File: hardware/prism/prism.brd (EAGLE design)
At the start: 100 x 79 mm, 164 parts, among them IC1 MAX3232CSE, IC2 XMEGA128-A1, IC3 NCV78M05BDTRKG, IC4 LM25011MY, IC5 74LVC4245APW, IC6 74LVC4245APW, IC7 LM2731XMF, J3 794618-4, K1 LED_G, K2 LED_G, K3 LED_G, K4 LED_G, K5 LED_G, K6 LED_G, K7 LED_G, K8 LED_G, T1 NTGS4111PT1G, T2 MMBT2222LT1G, T3 MMBT2222LT1G, T4 NTGS4111PT1G, T5 MMBT2222LT1G, T6 MMBT2222LT1G, T8 MMBT2222LT1G, T9 NTGS4111PT1G

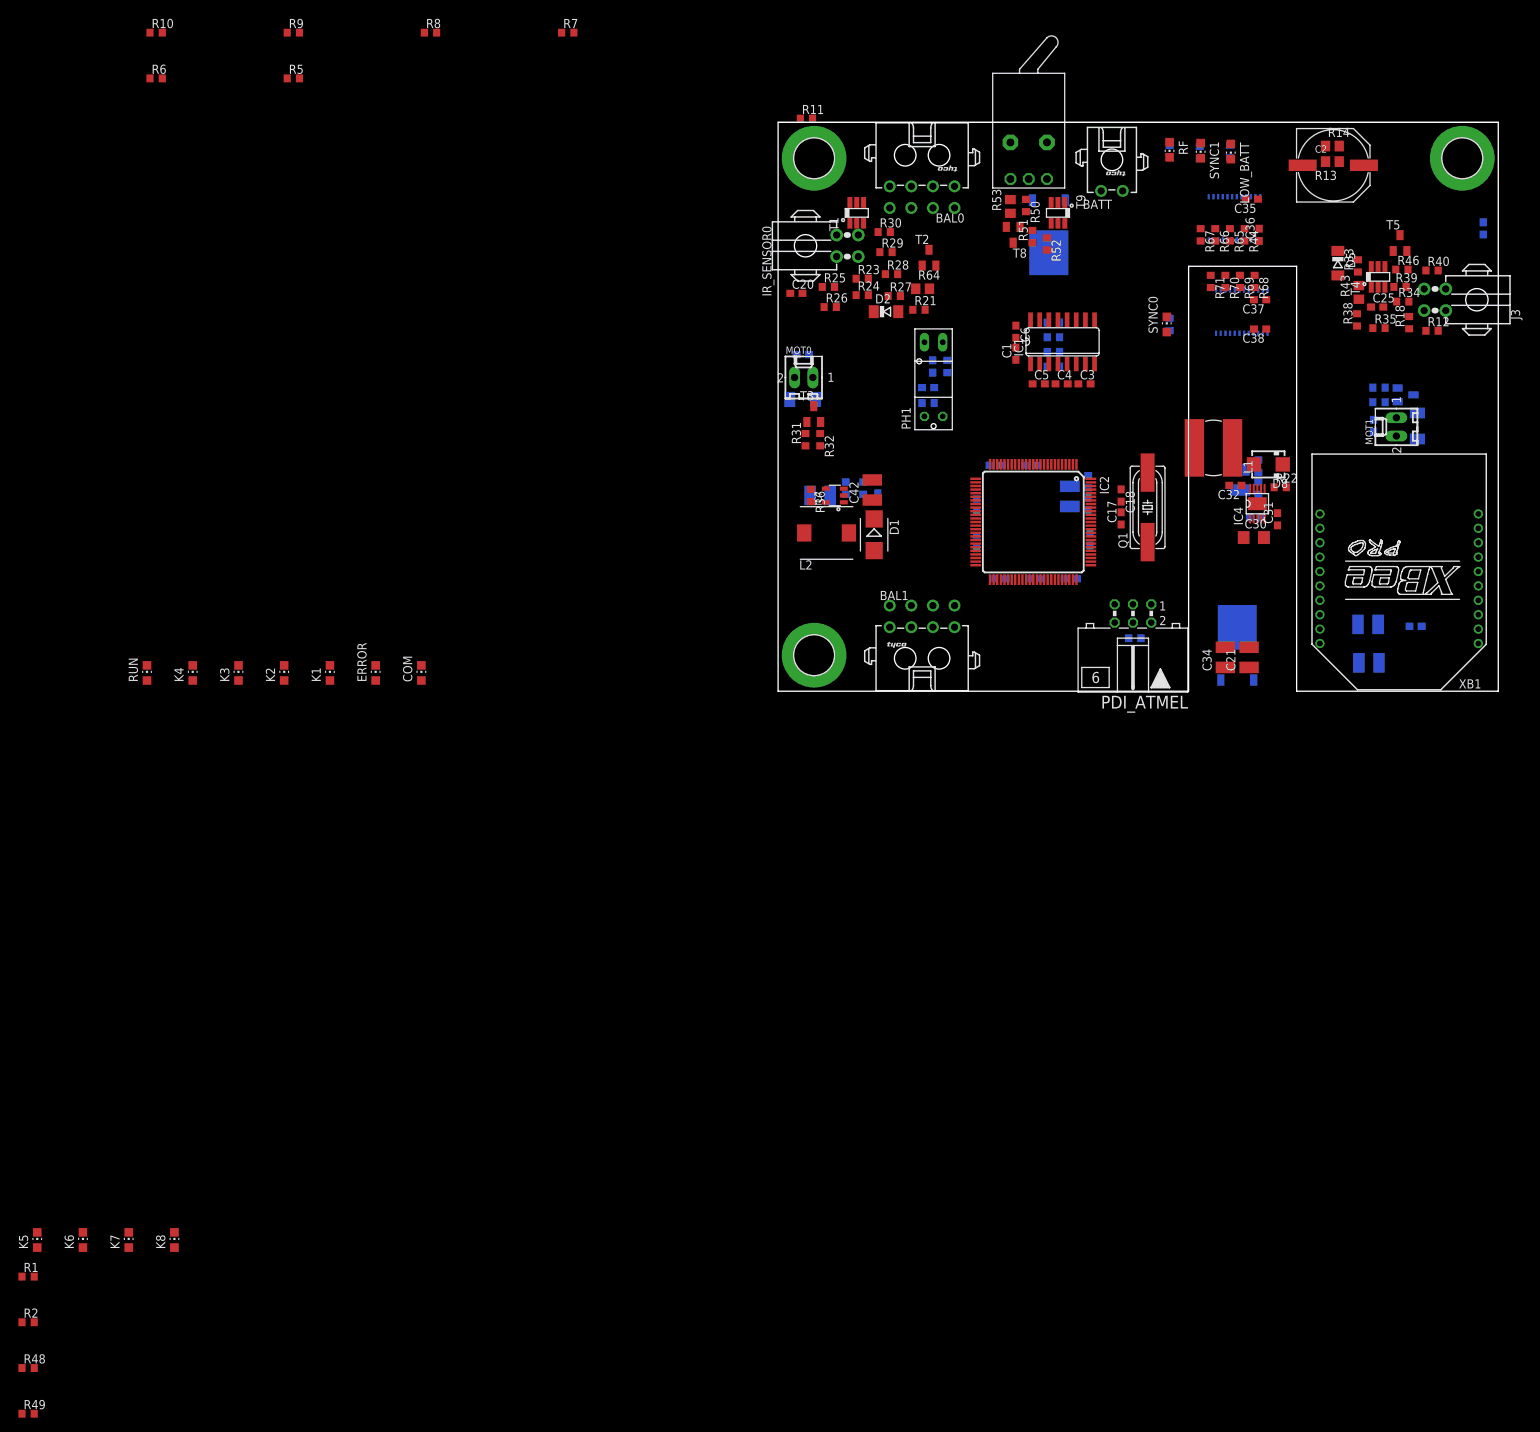
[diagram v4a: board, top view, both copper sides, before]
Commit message: added bluetooth board, begining of routing
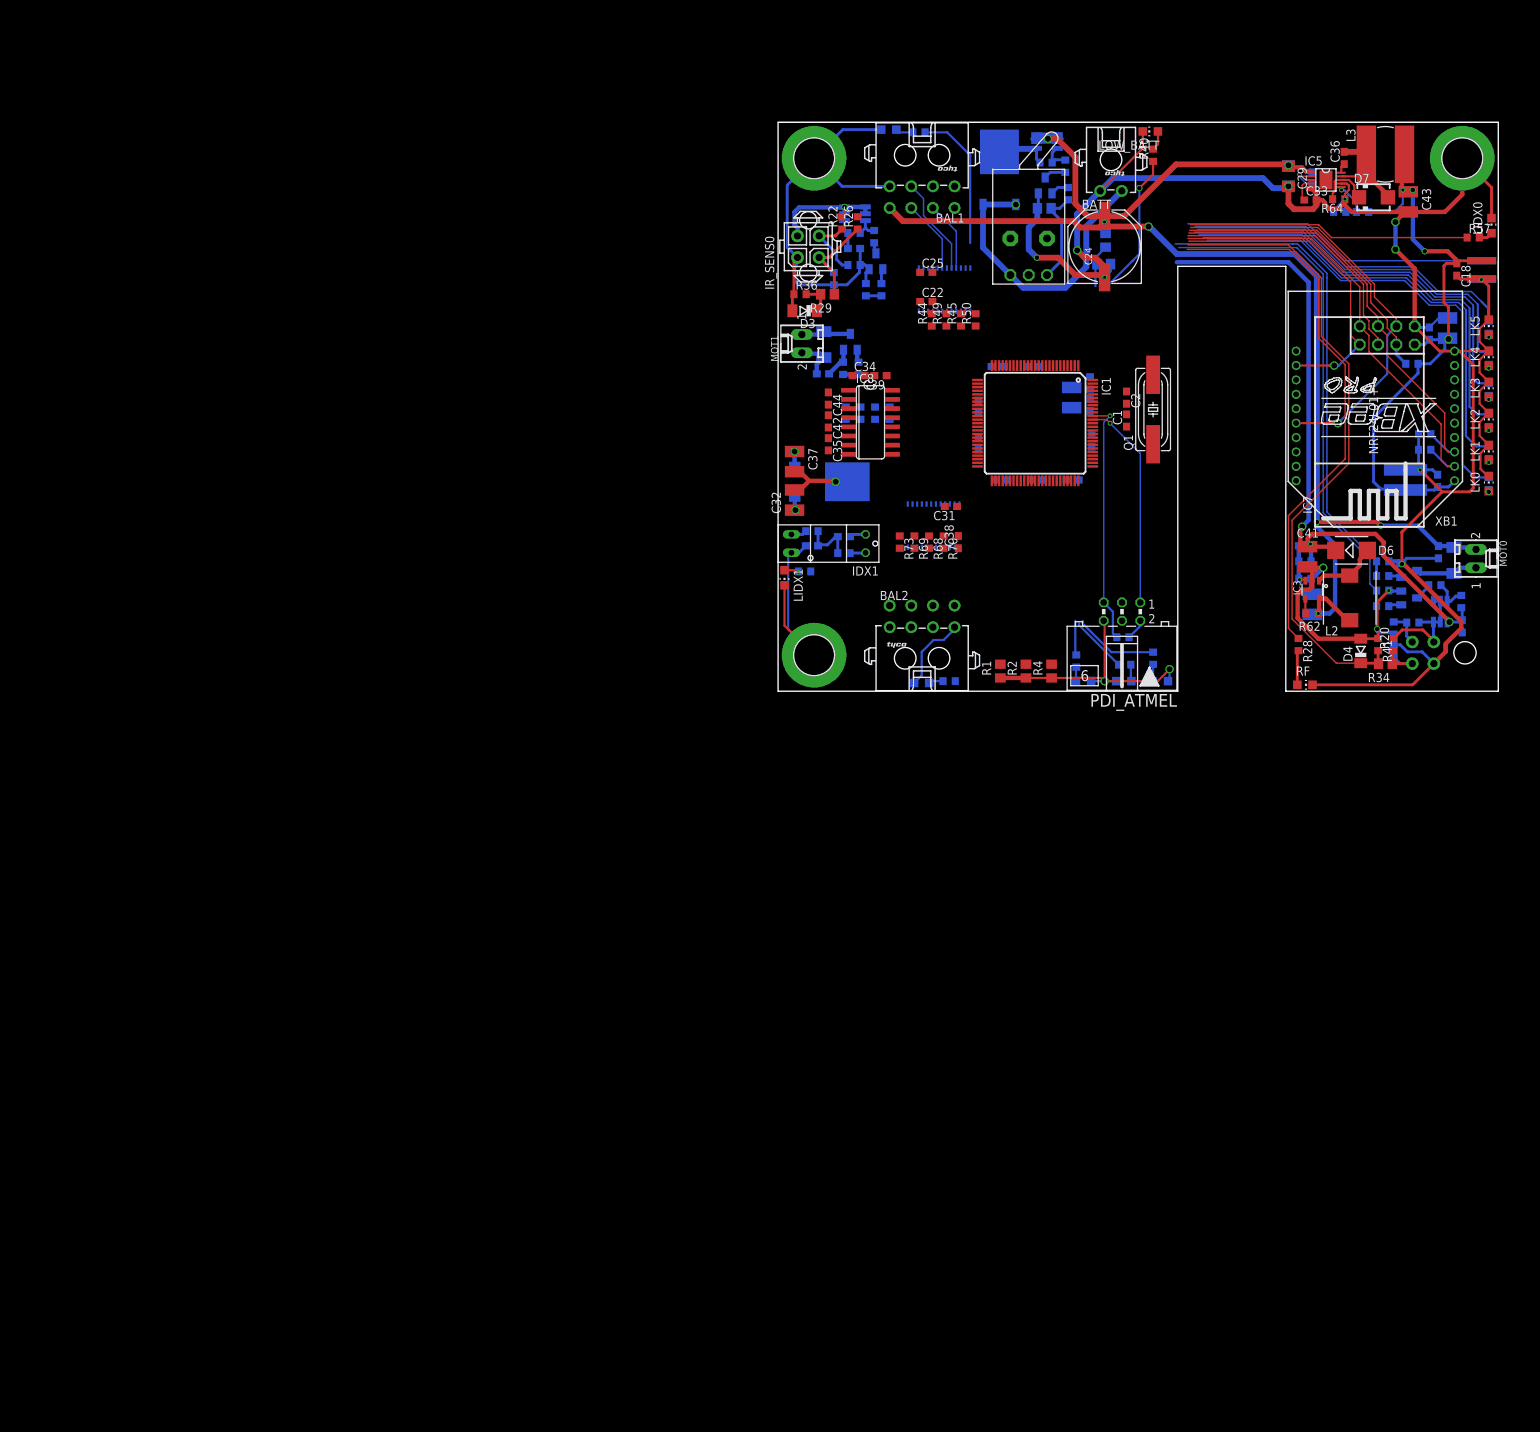
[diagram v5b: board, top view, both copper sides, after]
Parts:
- removed BAL0: 794618-8, robotter_connector:794618-8
- removed D8: B160-13F, robotter_diode:SMA
- removed IR_SENSOR0, J3: 794618-4, robotter_connector:794618-4
- removed K1, K2, K3, K4, K5, K6, K7, K8: LED_G, robotter_diode:CHIP-LED0805
- removed PH1: GP1S58VJ000F, robotter_ic:GP1S58VJ000F
- removed SYNC0: LED_B, robotter_diode:CHIP-LED0805
- removed T9: NTGS4111PT1G, robotter_ic:TSOP-6
- added BAL2: 794618-8, robotter_connector:794618-8
- added C26: 1µF 25V, robotter_capacitor:C1206
- added C44: 100nF 50V, robotter_capacitor:C0603
- added D4: bzv55-c3v3, robotter_diode:SOD80C
- added IC8: MAX3232CSE, robotter_ic:SO16
- added IDX0: PRISM_INDEX_EXTENSION_MALE, robotter_others:PRISM_INDEX_EXTENSION_MALE
- added IDX1: GP1S58VJ000F, robotter_ic:GP1S58VJ000F
- added IR_SENS0: 794681-4, robotter_connector:794681-4
- added IR_SENSOR1: 794618-4, robotter_connector:794618-4
- added LIDX0, LIDX1, LK0, LK1, LK2, LK3, LK4, LK5: LED_G, robotter_diode:CHIP-LED0805
- added R41: nc, rcl:R0603
- added R42, R72: 10K-F, robotter_resistor:R0603
- added R47, R59: 270-F, robotter_resistor:R0603
- added R73: 0-F, robotter_resistor:R0603
- added SYNC2: LED_B, robotter_diode:CHIP-LED0805
- added T7: MMBT2222LT1G, robotter_ic:SOT23-BEC
- C1: value 100nF 50V -> 15pF_0603_100V
- C15, C20, C32, C37: value 100nF 50V -> 10µF 25V; device robotter_capacitor:C0603 -> robotter_capacitor:C1210
- C17, C18: value 15pF_0603_100V -> 100nF 50V
- C2: value 330µF 35V -> 15pF_0603_100V; device robotter_capacitor:PANASONIC_G -> robotter_capacitor:C0603
- C22, C30: value 1µF 25V -> 100nF 50V; device robotter_capacitor:C1206 -> robotter_capacitor:C0603
- C24: value 100nF 50V -> 330µF 35V; device robotter_capacitor:C0603 -> robotter_capacitor:PANASONIC_G
- C29: value 100nF 50V -> 1µF 25V; device robotter_capacitor:C0603 -> robotter_capacitor:C1206
- C31: value 10nF 50V -> 100nF 50V
- C33: value 10µF 25V -> 10nF 50V; device robotter_capacitor:C1210 -> robotter_capacitor:C0603
- C34, C42, C8: value 10µF 25V -> 100nF 50V; device robotter_capacitor:C1210 -> robotter_capacitor:C0603
- C40: value 100nF 50V -> 180pF 50V
- C41: value 180pF 50V -> 10µF 25V; device robotter_capacitor:C0603 -> robotter_capacitor:C1210
- D1: value B120-13-F -> CGRM4004-G; device robotter_diode:SMB -> robotter_diode:SOD-123_MINI-SMA
- D2: value bzv55-c3v3 -> CGRM4004-G; device robotter_diode:SOD80C -> robotter_diode:SOD-123_MINI-SMA
- D3: value CGRM4004-G -> bzv55-c3v3; device robotter_diode:SOD-123_MINI-SMA -> robotter_diode:SOD80C
- D5: value bzv55-c3v3 -> (none); device robotter_diode:SOD80C -> robotter_diode:TO252
- D6: value CGRM4004-G -> B120-13-F; device robotter_diode:SOD-123_MINI-SMA -> robotter_diode:SMB
- D7: value (none) -> B160-13F; device robotter_diode:TO252 -> robotter_diode:SMA
- IC1: value MAX3232CSE -> XMEGA128-A1; device robotter_ic:SO16 -> avr-7:TQFP100
- IC2: value XMEGA128-A1 -> 74LVC4245APW; device avr-7:TQFP100 -> robotter_ic:TSSOP24
- IC3: value NCV78M05BDTRKG -> LM2731XMF; device linear:DPACK_3 -> robotter_ic:SOT23-5
- IC4: value LM25011MY -> 74LVC4245APW; device robotter_ic:MSOP10_THERMAL -> robotter_ic:TSSOP24
- IC5: value 74LVC4245APW -> LM25011MY; device robotter_ic:TSSOP24 -> robotter_ic:MSOP10_THERMAL
- IC6: value 74LVC4245APW -> NCV78M05BDTRKG; device robotter_ic:TSSOP24 -> linear:DPACK_3
- IC7: value LM2731XMF -> NRF24L01+; device robotter_ic:SOT23-5 -> robotter_ic:NRF24L01+
- L1: value SDR0805-270KL -> 220 ohms; device robotter_inductor:SDR0805 -> robotter_inductor:R0603
- L3: value 220 ohms -> SDR0805-270KL; device robotter_inductor:R0603 -> robotter_inductor:SDR0805
- R1, R2: value 270-F -> 0-E; device robotter_resistor:R0603 -> robotter_resistor:R0805
- R10, R11, R5, R54, R55, R7, R9: value 270-F -> 10K-F
- R12: value 0-F -> 1k
- R13: value 15k 1% -> 10K-F; device robotter_resistor:R0805 -> robotter_resistor:R0603
- R14: value 1k -> 10K-F; device robotter_resistor:R0805 -> robotter_resistor:R0603
- R16: value 4K7-F -> 1k
- R18: value 0-F -> 0; device robotter_resistor:R0603 -> rcl:R0603
- R19, R36: value 10K_1%-F -> nc; device robotter_resistor:R0603 -> rcl:R0603
- R20: value 113K-F -> 10K-F
- R22: value 0.27-F -> 0-F
- R23: value 10K-F -> 0-F
- R24: value 10K-F -> 4K7-F
- R25: value 0 -> 270-F; device rcl:R0603 -> robotter_resistor:R0603
- R27: value 1k -> nc; device robotter_resistor:R0603 -> rcl:R0603
- R28: value nc -> 270-F; device rcl:R0603 -> robotter_resistor:R0603
- R29, R34: value nc -> 4K7-E; device rcl:R0603 -> robotter_resistor:R0805
- R31, R38: value 1k -> 270-F
- R32, R35, R40, R52: value 10K-F -> 270-F
- R33: value nc -> 10K-F; device rcl:R0603 -> robotter_resistor:R0603
- R4: value 10K-F -> 0-E; device robotter_resistor:R0603 -> robotter_resistor:R0805
- R43: value 4K7-E -> 10K-F; device robotter_resistor:R0805 -> robotter_resistor:R0603
- R45: value 1k -> 0-F
- R46: value 10K-F -> 10K-E; device robotter_resistor:R0603 -> robotter_resistor:R0805
- R49: value 270-F -> 0-F
- R50: value 1K-F -> 0-F
- R51: value 10K-F -> 1K-F
- R53: value 10K-E -> 270-F; device robotter_resistor:R0805 -> robotter_resistor:R0603
- R58: value 75K-F -> 270-F
- R6, R8: value 270-F -> 1k
- R60: value 10K-F -> 15k 1%; device robotter_resistor:R0603 -> robotter_resistor:R0805
- R61: value 3K09-F -> 1k; device robotter_resistor:R0603 -> robotter_resistor:R0805
- R62: value 10K-F -> 10K_1%-F
- R63: value 10K-F -> 75K-F
- R64: value 4K7-E -> 0.27-F; device robotter_resistor:R0805 -> robotter_resistor:R0603
- R65: value 0-F -> 113K-F
- R66: value 0-F -> 10K_1%-F
- R67: value 0-F -> 10K-F
- R71: value 0-F -> 3K09-F
- T1, T4: value NTGS4111PT1G -> MMBT2222LT1G; device robotter_ic:TSOP-6 -> robotter_ic:SOT23-BEC
- T2, T5, T8: value MMBT2222LT1G -> NTGS4111PT1G; device robotter_ic:SOT23-BEC -> robotter_ic:TSOP-6
- moved R48 246.6 mm to (98.7, 46.2), flipped to the bottom, turned to 270 degrees
- moved R49 198.3 mm to (23.4, 51.6), turned to 90 degrees
- moved R10 193.4 mm to (91.2, 14.7), flipped to the bottom, turned to 180 degrees
- moved R6 185.4 mm to (83.9, 11.8), flipped to the bottom, turned to 180 degrees
- moved R9 180.4 mm to (94.9, 12.4), flipped to the bottom, turned to 270 degrees
- moved R5 167.1 mm to (83.9, 14.0), flipped to the bottom
- moved R2 165.5 mm to (34.4, 2.79), turned to 90 degrees
- moved R1 159.0 mm to (30.9, 2.79), turned to 90 degrees
- moved RUN 135.6 mm to (48.0, 1.40), flipped to the bottom, turned to 270 degrees
- moved COM 102.6 mm to (53.1, 1.40), flipped to the bottom, turned to 90 degrees
- moved ERROR 98.3 mm to (42.4, 1.40), flipped to the bottom, turned to 90 degrees
- moved MOT0 96.7 mm to (96.9, 18.4), turned to 270 degrees
- moved T1 93.5 mm to (87.6, 13.0), flipped to the bottom, turned to 90 degrees
- moved C43 91.3 mm to (87.5, 67.9), flipped to the top, turned to 270 degrees
- moved C23 89.9 mm to (91.6, 29.2), turned to 90 degrees
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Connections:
- removed net LED_SOUTH: IC2.68, R49.1, R8.1
- removed net N$21: K7.A, R48.2
- removed net N$93: K3.A, R7.2
- removed net XBEE_CTS_3V3: IC2.57, XB1.12
- removed net XBEE_RTS_3V3: IC2.58, XB1.16
- removed net XBEE_RX_3V3: IC2.31, XB1.2
- removed net XBEE_TX_3V3: IC2.32, XB1.3
- new net BEACON_ID_0_3V3: IC1.5, R1.2
- new net BEACON_ID_1_3V3: IC1.6, R2.2
- new net BEACON_ID_2_3V3: IC1.7, R4.2
- new net LED_INDEX_0_3V3: IC1.81, R57.1
- new net LED_INDEX_1_3V3: IC1.82, R59.1
- new net LK0_3V3: IC1.75, R47.1
- new net LK1: LK2.A, R56.2
- new net LK1_3V3: IC1.76, R52.1
- new net LK2_3V3: IC1.77, R56.1
- new net LK3_3V3: IC1.78, R58.1
- new net LK4_3V3: IC1.79, R48.1
- new net LK5: LIDX0.A, R57.2
- new net LK5_3V3: IC1.80, R53.1
- new net NRF_CSN_3V3: IC1.35, IC7.4, R67.1
- new net NRF_MOSI_3V3: IC1.30, IC7.6
- new net XBEE_CTS_3V3/NRF_IRQ_3V3: IC1.57, IC7.8, XB1.12
- new net XBEE_RTS_3V3/NRF_CE_3V3: IC1.58, IC7.3, XB1.16
- new net XBEE_RX_3V3/NRF_MISO_3V3: IC1.31, IC7.7, R43.2, XB1.2
- new net XBEE_TX_3V3/NRF_SCK_3V3: IC1.32, IC7.5, R42.2, XB1.3
- net +15V: now also C3.1, C4.1, C40.1, D6.C, R14.2, R65.1, R9.2, T2.4, T5.4; no longer C20.1, C25.1, C42.1, D1.C, R20.1, R24.2, R46.2, T1.4, T4.4
- net +3V3: now also C17.1, C18.1, C20.1, C21.1, C22.1, C23.1, C30.1, C31.1, C43.1, C5.1, C8.1, IC1.14, IC1.24, IC1.34, IC1.44, IC1.54, IC1.64, IC1.74, IC1.83, IC2.2, IC2.23, IC4.23, IC4.24, IC7.2, IC8.16, IDX0.2, R24.2, R3.1, R30.1, R33.1, R37.2, R39.2, R67.2, R71.1; no longer C10.1, C15.1, C28.1, C29.1, C33.1, C35.1, C37.1, C40.1, C6.1, IC1.16, IC2.14, IC2.34, IC2.44, IC2.54, IC2.64, IC2.74, IC2.83, IC5.2, IC5.23, IC5.24, IC6.23, IC6.24, R15.1, R16.2, R3.2, R4.2, R61.1, R62.1, R63.1
- net +5V: now also C25.1, C37.1, IC2.1, IC4.1, IC6.3; no longer C34.1, C36.1, IC3.3, IC5.1, IC6.1
- net /RESET_3V3: now also IC1.90, R3.2; no longer IC2.90, R15.2
- net BATTERY_MONITOR_0-1V: now also IC1.97, R60.1, R61.2; no longer IC2.97, R13.1, R14.2
- net GND: now also BAL2.1, C2.2, C24.-, C26.2, C32.2, C4.2, C41.2, C5.2, D3.A, D4.A, IC1.13, IC1.23, IC1.3, IC1.33, IC1.43, IC1.53, IC1.63, IC1.73, IC1.84, IC1.93, IC2.11, IC2.12, IC2.22, IC3.2, IC4.11, IC4.12, IC4.13, IC4.2, IC4.22, IC5.5, IC5.7, IC6.4, IC7.1, IC8.15, IDX0.1, IDX0.3, IDX1.LED_C, IDX1.TRANSISTOR_E, IR_SENS0.1, IR_SENSOR1.1, LIDX0.C, LIDX1.C, LK0.C, LK1.C, LK2.C, LK3.C, LK4.C, LK5.C, R1.1, R11.1, R13.1, R2.1, R23.1, R27.1, R36.1, R4.1, R41.1, R42.1, R43.1, R46.1, R5.1, R61.1, R64.1, R66.1, R7.1, R72.2, SYNC2.C, T1.E, T4.E, T7.E; no longer BAL0.1, C2.-, C24.2, C36.2, C40.2, C42.2, D2.A, D5.A, IC1.15, IC2.23, IC2.3, IC2.33, IC2.43, IC2.53, IC2.63, IC2.73, IC2.84, IC2.93, IC3.4, IC4.5, IC4.7, IC5.11, IC5.12, IC5.13, IC5.22, IC6.11, IC6.12, IC6.13, IC6.2, IC6.22, IC7.2, IR_SENSOR0.1, J3.1, K1.C, K2.C, K3.C, K4.C, K5.C, K6.C, K7.C, K8.C, PH1.LED_C, PH1.TRANSISTOR_E, R14.1, R18.1, R22.1, R28.1, R29.1, R30.1, R32.1, R33.1, R34.1, R35.1, R37.1, R53.1, R60.2, SYNC0.C, T2.E, T5.E, T8.E
- net INT0_0_3V3: now also IC4.16, R50.1; no longer IC6.16, R71.1
- net INT0_0_5V: now also BAL1.2, IC2.8, R73.2; no longer BAL0.2, IC5.8, R67.2
- net INT0_1_3V3: now also IC4.17, R45.1; no longer IC6.17, R70.1
- net INT0_1_5V: now also BAL2.2, IC2.7, R69.2; no longer BAL1.2, IC5.7, R66.2
- net INT1_0_3V3: now also IC4.18, R49.1; no longer IC6.18, R69.1
- net INT1_0_5V: now also BAL1.6, IC2.6, R68.2; no longer BAL0.6, IC5.6, R65.2
- net INT1_1_3V3: now also IC4.19, R44.1; no longer IC6.19, R68.1
- net INT1_1_5V: now also BAL2.6, IC2.5, R70.2; no longer BAL1.6, IC5.5, R44.2
- net IR_SENSOR_0_OUTPUT_24V: now also IR_SENSOR1.2, R20.1, R21.2, R34.1; no longer IR_SENSOR0.2, R23.1, R28.2, R64.1
- net IR_SENSOR_0_OUTPUT_3V3: now also D3.C, IC1.17, R29.2, R36.2; no longer D2.C, IC2.17, R21.2, R64.2
- net IR_SENSOR_1_OUTPUT_24V: now also IR_SENS0.2, R26.1, R27.2, R29.1; no longer J3.2, R34.2, R39.1, R43.1
- net IR_SENSOR_1_OUTPUT_3V3: now also D4.C, IC1.37, R34.2, R41.2; no longer D5.C, IC2.37, R33.2, R43.2
- net LED_EAST: now also IC1.56; no longer IC2.56, R2.1, R6.1
- net LED_NORTH: now also IC1.62; no longer IC2.62, R1.1, R5.1
- net LED_WEST: now also IC1.95; no longer IC2.95, R48.1, R7.1
- net MIRROR_INDEX_0_3V3: now also IC1.18, IDX0.4; no longer IC2.18, PH1.TRANSISTOR_C, R16.1
- net MIRROR_INDEX_1_3V3: now also IC1.38, IDX1.TRANSISTOR_C, R24.1; no longer IC2.38
- net MOTOR_M_0: now also D2.A, T6.C; no longer D3.A, T3.C
- net MOTOR_M_1: now also D1.A, T4.C; no longer D6.A, T6.C
- net MOTOR_PWM_0_3V3: now also IC1.25, R13.2, R16.1; no longer IC2.25, R31.1, R32.2
- net MOTOR_PWM_1_3V3: now also IC1.26, R11.2, R12.1; no longer IC2.26, R37.2, R45.1
- net N$1: now also C44.1, IC8.1; no longer C5.1, IC1.1
- net N$10: now also IC1.71, R31.1; no longer IC2.76, R10.1
- net N$11: now also C34.1, IC8.2; no longer C1.1, IC1.2
- net N$12: now also IC1.72, R35.1; no longer IC2.77, R11.1
- net N$128: now also R10.2, R9.1, T2.3; no longer R24.1, R26.2, T1.3
- net N$129: now also IR_SENSOR1.4, R18.1, R19.2; no longer IR_SENSOR0.4, R25.1, R29.2
- net N$13: now also C35.1, IC8.6; no longer C3.1, IC1.6
- net N$14: now also R14.1, R15.2, T5.3; no longer R40.2, R46.1, T4.3
- net N$16: now also R8.2, T3.B; no longer R38.2, T5.B
- net N$17: now also R15.1, T3.C; no longer R40.1, T5.C
- net N$18: now also R16.2; no longer R45.2
- net N$19: now also LK0.A, R47.2; no longer K5.A, R1.2
- net N$2: now also R25.2; no longer R9.2
- net N$20: now also LK1.A, R52.2; no longer K6.A, R2.2
- net N$22: now also LK3.A, R58.2; no longer K8.A, R49.2
- net N$23: now also D5.1, D5.3, SW_BATT.1; no longer D7.1, D7.3, SW_BATT.2
- net N$24: now also C42.2, IC8.5; no longer C4.2, IC1.5
- net N$25: now also R51.2, T7.B; no longer R50.2, T8.B
- net N$26: now also R54.1, R55.2, T8.3; no longer R51.2, R52.1, T9.3
- net N$27: now also R28.2; no longer R54.2
- net N$28: now also IC1.65, R28.1; no longer IC2.69, R54.1
- net N$29: now also R55.1, T7.C; no longer R51.1, T8.C
- net N$3: now also R12.2, T4.B; no longer R31.2, T3.B
- net N$30: now also D5.4, R54.2, T8.4; no longer D7.4, R52.2, T9.4
- net N$31: now also IC1.67, R38.2; no longer IC2.71, R55.2
- net N$32: now also IC1.68, R40.1; no longer IC2.72, R56.1
- net N$33: now also R38.1, SYNC2.A; no longer R55.1, SYNC1.A
- net N$34: now also R40.2; no longer R56.2
- net N$35: now also R32.1, SYNC1.A; no longer R57.1, SYNC0.A
- net N$36: now also IC1.66, R32.2; no longer IC2.70, R57.2
- net N$37: now also R6.2, T1.B; no longer R27.2, T2.B
- net N$38: now also C36.2, D7.A, IC5.9, L3.1; no longer C32.2, D8.A, IC4.9, L1.1
- net N$39: now also D7.C, IC5.8, R64.2; no longer D8.C, IC4.8, R22.2
- net N$4: now also R31.2; no longer R10.2
- net N$40: now also IC5.2, R63.1; no longer IC4.2, R58.1
- net N$41: now also IR_SENS0.4, R22.1, R23.2; no longer J3.4, R12.1, R18.2
- net N$42: now also R10.1, T1.C; no longer R26.1, T2.C
- net N$43: now also C33.1, IC5.4; no longer C31.1, IC4.4
- net N$44: now also IC5.6, R71.2, R72.1; no longer IC4.6, R60.1, R61.2
- net N$45: now also C1.1, IC1.91; no longer C17.1, IC2.91
- net N$46: now also C2.1, IC1.92; no longer C18.1, IC2.92
- net N$47: now also IC4.5, R70.1; no longer IC6.5, R44.1
- net N$48: now also C36.1, IC5.10; no longer C32.1, IC4.10
- net N$49: now also IC2.19, R44.2; no longer IC5.19, R68.2
- net N$5: now also C44.2, IC8.3; no longer C5.2, IC1.3
- net N$50: now also IC2.17, R45.2; no longer IC5.17, R70.2
- net N$51: now also IC2.18, R49.2; no longer IC5.18, R69.2
- net N$52: now also IC2.16, R50.2; no longer IC5.16, R71.2
- net N$53: now also IC4.6, R68.1; no longer IC6.6, R65.1
- net N$54: now also IC4.8, R73.1; no longer IC6.8, R67.1
- net N$55: now also IC4.7, R69.1; no longer IC6.7, R66.1
- net N$56: now also IR_SENSOR1.3, R18.2, R20.2, T2.1, T2.2, T2.5, T2.6; no longer IR_SENSOR0.3, R23.2, R25.2, T1.1, T1.2, T1.5, T1.6
- net N$57: now also IDX1.LED_A; no longer PH1.LED_A
- net N$58: now also IR_SENS0.3, R22.2, R26.2, T5.1, T5.2, T5.5, T5.6; no longer J3.3, R12.2, R39.2, T4.1, T4.2, T4.5, T4.6
- net N$59: now also D6.A, IC3.1; no longer D1.A, IC7.1
- net N$6: now also C42.1, IC8.4; no longer C4.1, IC1.4
- net N$60: now also C40.2, IC3.3, R65.2, R66.2; no longer C41.2, IC7.3, R19.2, R20.2
- net N$63: now also IC3.4, R62.1; no longer IC7.4, R36.1
- net N$7: now also R35.2; no longer R11.2
- net N$8: now also C10.1, C15.1, IC1.4, IC1.94, L1.1; no longer C7.1, C8.1, IC2.4, IC2.94, L3.1
- net N$9: now also IC1.70, R25.1; no longer IC2.75, R9.1
- net N$91: now also LK4.A, R48.2; no longer K1.A, R5.2
- net N$92: now also LK5.A, R53.2; no longer K2.A, R6.2
- net N$94: now also LIDX1.A, R59.2; no longer K4.A, R8.2
- net ON/OFF_SENSOR_0_3V3: now also IC1.27, R7.2, R8.1; no longer IC2.28, R27.1, R30.2
- net ON/OFF_SENSOR_1_3V1: now also R46.2, R51.1, SW_BATT.3; no longer R50.1, R53.2, SW_BATT.1
- net ON/OFF_SENSOR_1_3V3: now also IC1.28, R5.2, R6.1; no longer IC2.29, R35.2, R38.1
- net PDI_DATA_3V3: now also IC1.89; no longer IC2.89
- net RX_0_3V3: now also IC1.51, IC8.12, R37.1; no longer IC1.12, IC2.51, R3.1
- net RX_0_RS232: now also BAL1.8, IC8.13; no longer BAL0.8, IC1.13
- net RX_1_3V3: now also IC1.47, IC8.9, R30.2; no longer IC1.9, IC2.47, R62.2
- net RX_1_RS232: now also BAL2.8, IC8.8; no longer BAL1.8, IC1.8
- net SYNC_IN_0_3V3: now also IC1.19, IC2.15; no longer IC2.19, IC5.15
- net SYNC_IN_0_5V: now also BAL1.7, IC2.9; no longer BAL0.7, IC5.9
- net SYNC_IN_1_3V3: now also IC1.20, IC2.14; no longer IC2.20, IC5.14
- net SYNC_IN_1_5V: now also BAL2.7, IC2.10; no longer BAL1.7, IC5.10
- net SYNC_OUT_0_3V3: now also IC1.21, IC4.15; no longer IC2.21, IC6.15
- net SYNC_OUT_0_5V: now also BAL1.3, IC4.9; no longer BAL0.3, IC6.9
- net SYNC_OUT_1_3V3: now also IC1.22, IC4.14; no longer IC2.22, IC6.14
- net SYNC_OUT_1_5V: now also BAL2.3, IC4.10; no longer BAL1.3, IC6.10
- net TX_0_3V3: now also IC1.52, IC8.11, R39.1; no longer IC1.11, IC2.52, R4.1
- net TX_0_RS232: now also BAL1.4, IC8.14; no longer BAL0.4, IC1.14
- net TX_1_3V3: now also IC1.48, IC8.10, R33.2; no longer IC1.10, IC2.48, R63.2
- net TX_1_RS232: now also BAL2.4, IC8.7; no longer BAL1.4, IC1.7
- net VBAT: now also BAL2.5, C24.+, C26.1, C28.1, C29.1, C32.1, C6.1, C7.1, D1.C, D2.C, IC3.5, IC5.1, IC6.1, R60.2, R62.2, R63.2, T8.1, T8.2, T8.5, T8.6; no longer BAL0.5, C2.+, C21.1, C22.1, C23.1, C24.1, C30.1, C43.1, D3.C, D6.C, IC3.1, IC4.1, IC7.5, R13.2, R36.2, R58.2, T9.1, T9.2, T9.5, T9.6
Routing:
- net GND: track 0.00 -> 520.7 mm, vias 0 -> 16
- net VBAT: track 0.00 -> 223.9 mm, vias 0 -> 8
- net +15V: track 0.00 -> 99.9 mm, vias 0 -> 3
- net +3V3: track 0.00 -> 94.9 mm, vias 0 -> 4
- net IR_SENSOR_1_OUTPUT_3V3: track 0.00 -> 89.0 mm
- net N$28: track 0.00 -> 75.3 mm
- net ON/OFF_SENSOR_1_3V3: track 0.00 -> 70.8 mm
- net MOTOR_PWM_0_3V3: track 0.00 -> 67.7 mm
- net LK0_3V3: track 0.00 -> 65.2 mm
- net LK1_3V3: track 0.00 -> 61.9 mm
- net XBEE_RX_3V3/NRF_MISO_3V3: track 0.00 -> 61.8 mm
- net XBEE_TX_3V3/NRF_SCK_3V3: track 0.00 -> 60.8 mm
- net LK2_3V3: track 0.00 -> 58.6 mm
- net XBEE_RTS_3V3/NRF_CE_3V3: track 0.00 -> 58.5 mm, vias 0 -> 1
- net LK3_3V3: track 0.00 -> 55.5 mm
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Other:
- outline, holes or cut-outs redrawn

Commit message: bord routed, ready to review
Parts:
- moved R70 13.5 mm to (14.0, 30.7), flipped to the bottom, turned to 90 degrees
- moved R68 11.2 mm to (16.0, 30.7), flipped to the bottom, turned to 90 degrees
- moved R73 10.5 mm to (20.1, 30.7), flipped to the bottom, turned to 90 degrees
- moved R69 10.1 mm to (18.0, 30.7), flipped to the bottom, turned to 90 degrees
- moved R37 6.48 mm to (9.02, 38.5)
- moved R30 3.69 mm to (15.1, 38.5)
- moved R33 3.69 mm to (13.1, 38.5)
- moved R20 3.58 mm to (85.1, 2.92), turned to 0 degrees
- moved R34 2.95 mm to (85.6, 6.48), turned to 90 degrees
- moved R22 2.90 mm to (7.11, 67.3), turned to 0 degrees
- moved R44 2.73 mm to (20.1, 49.1), flipped to the bottom
- moved R45 2.73 mm to (24.1, 49.1), flipped to the bottom
- moved R49 2.73 mm to (22.1, 49.1), flipped to the bottom
- moved R50 2.73 mm to (26.2, 49.1), flipped to the bottom
- moved R39 2.42 mm to (11.0, 38.5)
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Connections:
- removed net LED_EAST: IC1.56
- removed net LED_NORTH: IC1.62
- removed net LED_WEST: IC1.95
- removed net N$32: IC1.68, R40.1
- removed net N$36: IC1.66, R32.2
- new net LOW_BAT_LED_3V3: IC1.36, R40.1
- new net SYNC1_LED_3V3: IC1.35, R32.2
- net BEACON_ID_0_3V3: now also IC1.57; no longer IC1.5
- net BEACON_ID_1_3V3: now also IC1.58; no longer IC1.6
- net BEACON_ID_2_3V3: now also IC1.59; no longer IC1.7
- net INT0_0_3V3: now also IC1.39, IC4.17; no longer IC4.16
- net INT0_1_3V3: now also IC1.40, IC4.16; no longer IC4.17
- net INT1_0_3V3: now also IC1.41, IC4.15; no longer IC4.18
- net INT1_1_3V3: now also IC1.42, IC4.14; no longer IC4.19
- net IR_SENSOR_0_OUTPUT_3V3: now also IC1.30; no longer IC1.17
- net IR_SENSOR_1_OUTPUT_3V3: now also IC1.15; no longer IC1.37
- net LED_INDEX_0_3V3: now also IC1.6; no longer IC1.81
- net LED_INDEX_1_3V3: now also IC1.55; no longer IC1.82
- net LK0_3V3: now also IC1.7; no longer IC1.75
- net LK1_3V3: now also IC1.8; no longer IC1.76
- net LK2_3V3: now also IC1.9; no longer IC1.77
- net LK3_3V3: now also IC1.10; no longer IC1.78
- net LK4_3V3: now also IC1.11; no longer IC1.79
- net LK5_3V3: now also IC1.12; no longer IC1.80
- net MIRROR_INDEX_0_3V3: now also IC1.29; no longer IC1.18
- net MIRROR_INDEX_1_3V3: now also IC1.18, IC1.19; no longer IC1.38
- net N$10: now also IC1.60; no longer IC1.71
- net N$12: now also IC1.62; no longer IC1.72
- net N$23: now also SW_BATT.2; no longer SW_BATT.1
- net N$28: now also IC1.1; no longer IC1.65
- net N$31: now also IC1.56; no longer IC1.67
- net N$47: now also IC4.10; no longer IC4.5
- net N$53: now also IC4.9; no longer IC4.6
- net N$54: now also IC4.7; no longer IC4.8
- net N$55: now also IC4.8; no longer IC4.7
- net N$9: now also IC1.61; no longer IC1.70
- net NRF_CSN_3V3: now also IC1.2; no longer IC1.35
- net NRF_MOSI_3V3: now also IC1.20; no longer IC1.30
- net ON/OFF_SENSOR_0_3V3: now also IC1.32; no longer IC1.27
- net ON/OFF_SENSOR_1_3V3: now also IC1.17; no longer IC1.28
- net RX_0_3V3: now also IC1.47, R30.2; no longer IC1.51, R37.1
- net RX_1_3V3: now also IC1.51, R37.1; no longer IC1.47, R30.2
- net SYNC_IN_0_3V3: now also IC1.27; no longer IC1.19
- net SYNC_IN_1_3V3: now also IC1.31; no longer IC1.20
- net SYNC_OUT_0_3V3: now also IC1.50, IC4.21; no longer IC1.21, IC4.15
- net SYNC_OUT_0_5V: now also IC4.3; no longer IC4.9
- net SYNC_OUT_1_3V3: now also IC1.49, IC4.20; no longer IC1.22, IC4.14
- net SYNC_OUT_1_5V: now also IC4.4; no longer IC4.10
- net TX_0_3V3: now also IC1.48, R33.2; no longer IC1.52, R39.1
- net TX_1_3V3: now also IC1.52, R39.1; no longer IC1.48, R33.2
- net XBEE_CTS_3V3/NRF_IRQ_3V3: now also IC1.16; no longer IC1.57
- net XBEE_RTS_3V3/NRF_CE_3V3: now also IC1.5; no longer IC1.58
- net XBEE_RX_3V3/NRF_MISO_3V3: now also IC1.21; no longer IC1.31
- net XBEE_TX_3V3/NRF_SCK_3V3: now also IC1.22; no longer IC1.32
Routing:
- net +3V3: track 94.9 -> 398.7 mm, vias 4 -> 23
- net GND: track 520.7 -> 811.7 mm, vias 16 -> 57
- net VBAT: track 223.9 -> 338.3 mm, vias 8 -> 13
- net +5V: track 2.94 -> 75.5 mm, vias 1 -> 7
- net +15V: track 99.9 -> 161.7 mm, vias 3 -> 7
- net SYNC_OUT_0_5V: track 0.00 -> 61.5 mm, vias 0 -> 2
- net INT0_1_5V: track 0.00 -> 60.1 mm, vias 0 -> 2
- net INT1_1_5V: track 0.00 -> 59.1 mm
- net LOW_BAT_LED_3V3: track 0.00 -> 56.7 mm, vias 0 -> 4
- net MIRROR_INDEX_1_3V3: track 2.18 -> 57.5 mm, vias 0 -> 2
- net RX_0_RS232: track 0.00 -> 54.4 mm, vias 0 -> 1
- net SYNC_IN_1_5V: track 0.00 -> 54.1 mm, vias 0 -> 2
- net SYNC1_LED_3V3: track 0.00 -> 51.0 mm, vias 0 -> 3
- net MIRROR_INDEX_0_3V3: track 42.9 -> 92.6 mm, vias 0 -> 1
- net TX_0_RS232: track 0.00 -> 44.1 mm, vias 0 -> 1
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- added copper zone on layer 1, net GND
- added copper zone on layer 16, net GND
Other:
- board text added: "+"
- board text added: "-"
- board text added: "beacon_id2 -> R4 beacon_id1 -> R2 beacon_id0 -> R1"
- board text added: "on<>off"
- board text added: "prism_V1 Ro'otter 2014"
